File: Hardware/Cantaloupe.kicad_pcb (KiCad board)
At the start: 2 copper layers, 289.7 x 117 mm, 167 parts, among them J1 OLED, J2 Interconnect, J3 ICSP, J4 BAT_CON, J5 BAT_CON_R, J6 OLED, J7 Interconnect_R, J8 ICSP_R, J9 BAT_CON_TOG, SW1 MX, SW10 MX, SW11 MX, SW12 MX, SW13 MX, SW14 MX, SW15 MX, SW16 MX, SW17 MX, SW18 MX, SW19 MX, SW2 MX, SW20 MX, SW21 MX, SW22 MX, SW23 MX, SW24 MX, SW25 MX, SW26 MX, SW27 MX, SW28 MX, SW29 MX, SW3 MX, SW30 MX, SW31 MX, SW32 MX, SW33 Encoder, SW34 MX, SW35 Reset, SW36 BAT_TOG, SW37 MX, SW38 MX, SW39 MX, SW4 MX, SW40 MX, SW41 MX, SW42 MX, SW43 MX, SW44 MX, SW45 MX, SW46 MX, SW47 MX, SW48 MX, SW49 MX, SW5 MX, SW50 MX, SW51 MX, SW52 MX, SW53 MX, SW54 MX, SW55 MX, SW56 MX, SW57 MX, SW58 MX, SW59 MX, SW6 MX, SW60 MX, SW61 MX, SW62 MX, SW63 MX, SW64 MX, SW65 MX, SW66 MX, SW67 MX, SW68 MX, SW69 Encoder_R, SW7 MX, SW70 MX, SW71 Reset, SW72 BAT_TOG_R, SW8 MX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

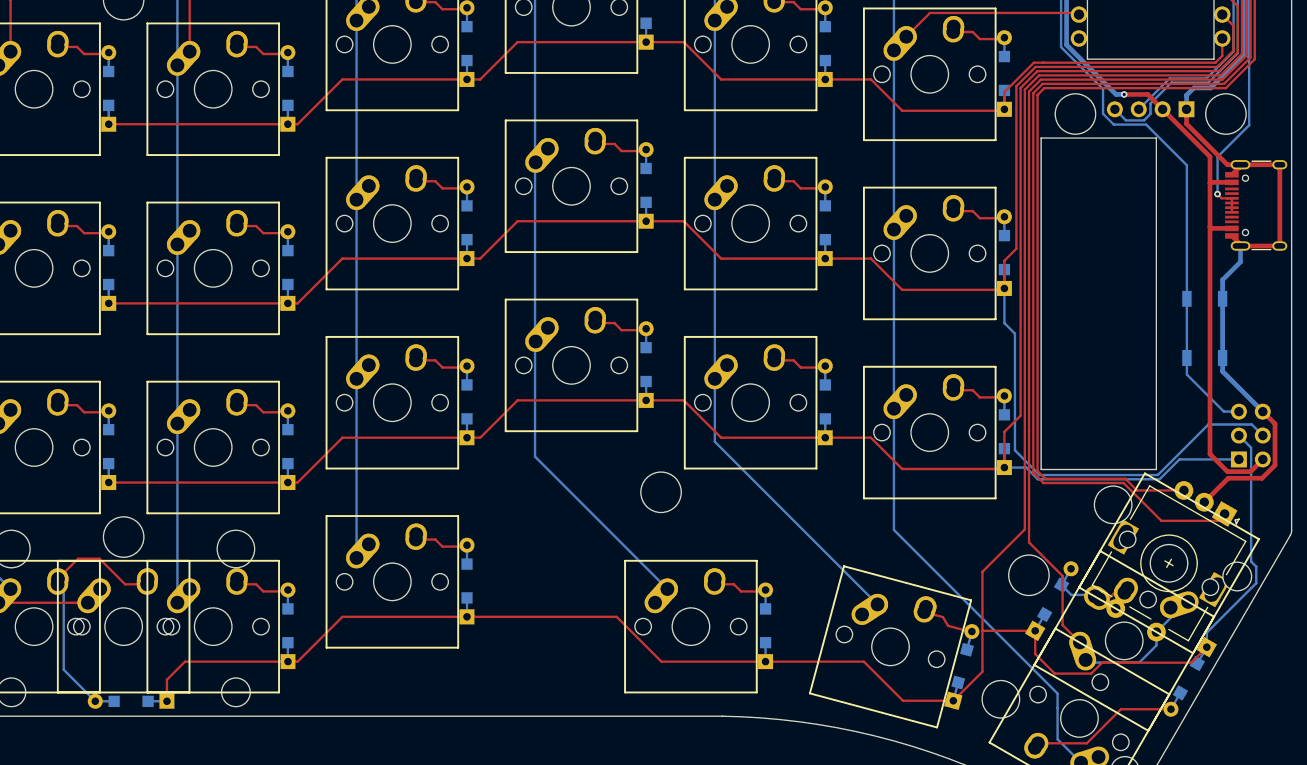
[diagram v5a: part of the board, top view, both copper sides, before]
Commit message: Updated position of diode
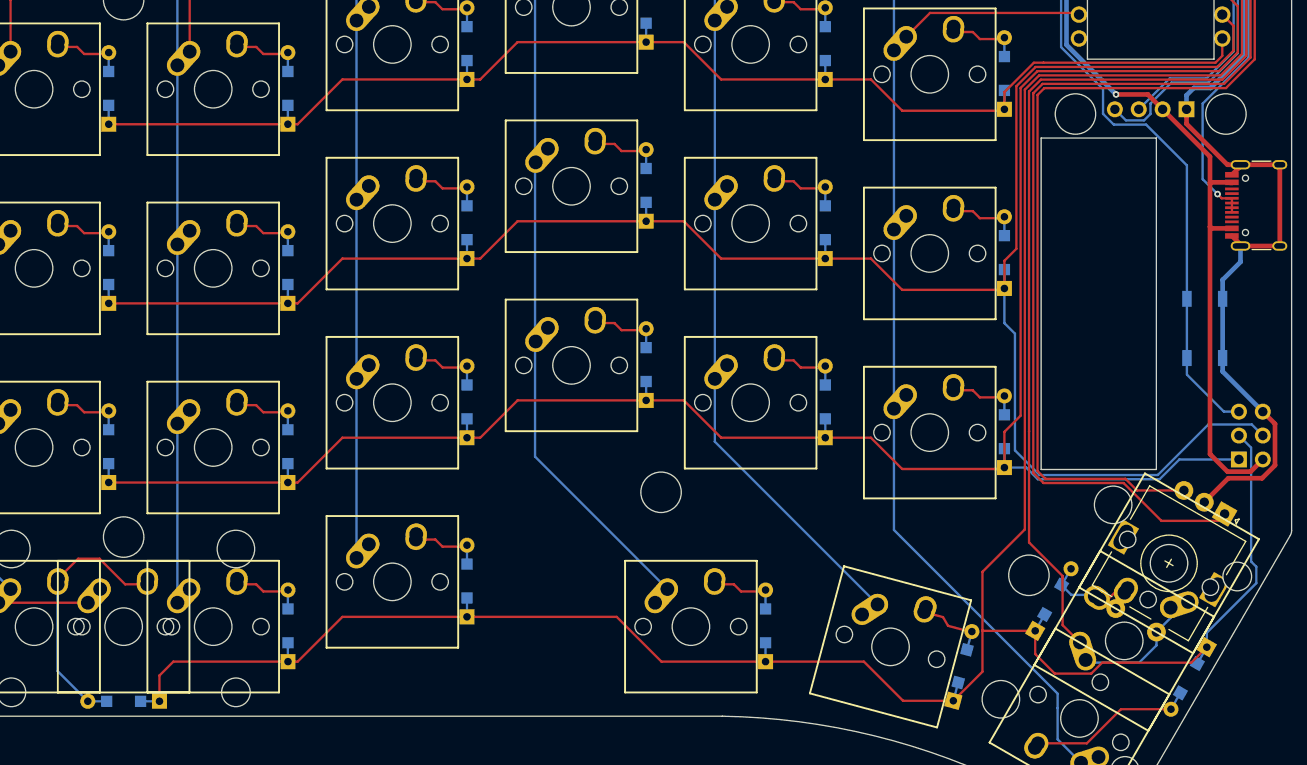
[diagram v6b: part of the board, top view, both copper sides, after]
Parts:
- moved D25 0.79 mm to (215.9, 134.9)
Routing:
- net DATA: track 47.7 -> 49.0 mm
- net ROW4: track 263.2 -> 264.3 mm

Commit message: Changed OLED support to 0.96" OLED
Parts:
- removed the REF** at (319.6, 92.7)
- removed the REF** at (333.1, 72.5)
- removed the REF** at (317.1, 72.5)
- removed the REF** at (70.9, 92.7)
- removed the REF** at (57.4, 72.5)
- removed the REF** at (73.4, 72.5)
- J1, J6: footprint Cantaloupe:PinHeader_1x04_P2.54mm_Vertical_No_Silk -> Cantaloupe:OLED_0.96_SSD1306_128x64
- SW35, SW71: moved to F.Cu
- moved J2 18.0 mm to (337.8, 100.2)
- moved J7 18.0 mm to (52.7, 100.2)
- moved SW35 7.07 mm to (325.9, 100.3)
- moved SW71 7.07 mm to (64.6, 100.3), turned to 270 degrees
- moved J8 6.98 mm to (57.8, 110.9), turned to 90 degrees
- moved J3 3.70 mm to (337.8, 110.9), turned to 90 degrees
- moved J6 3.56 mm to (64.2, 68.7), turned to 0 degrees
- moved J1 3.55 mm to (326.4, 68.7), turned to 0 degrees
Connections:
- U1 pad 4: GND1 -> Net-(U1-Pad4)
- U2 pad 4: GND2 -> Net-(U2-Pad4)
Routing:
- net GND1: track 101.8 -> 133.8 mm
- net GND2: track 140.7 -> 120.3 mm
- net ROW2: track 212.8 -> 196.5 mm
- net DATA: track 49.0 -> 64.8 mm
- net COL5_R: track 156.1 -> 142.1 mm
- net RESET: track 74.1 -> 86.5 mm, vias 0 -> 3
- net DATA_R: track 58.8 -> 70.9 mm
- net SDA: track 37.2 -> 25.6 mm
- net SDA_R: track 36.9 -> 27.4 mm
- net VDD: track 83.1 -> 74.0 mm, vias 0 -> 2
- net ROW4: track 264.3 -> 257.3 mm
- net COL4_R: track 172.0 -> 166.3 mm
- net RESET_R: track 82.0 -> 87.5 mm, vias 0 -> 4
- net SCL: track 29.7 -> 24.9 mm
- net VCC: track 85.3 -> 81.8 mm
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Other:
- board text removed: "OLED"

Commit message: Changed orientation of 1u switches in thumb cluster. Updated plate to add 2u support.
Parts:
- turned SW30 to 60 degrees
- turned SW34 to 60 degrees
- turned SW61 to 300 degrees
- turned SW70 to 300 degrees
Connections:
- SW34 pad 1: PERIPH -> Net-(D31-Pad2)
- SW34 pad 2: Net-(D31-Pad2) -> PERIPH
- SW70 pad 1: PERIPH_R -> Net-(D62-Pad2)
- SW70 pad 2: Net-(D62-Pad2) -> PERIPH_R
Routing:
- net PERIPH: track 109.9 -> 119.7 mm
- net Net-(D62-Pad2): track 22.7 -> 30.7 mm
- net COL5: track 122.5 -> 116.0 mm
- net Net-(D56-Pad2): track 14.9 -> 18.4 mm
- net ROW4: track 257.3 -> 259.9 mm
- net COL5_R: track 142.1 -> 139.7 mm
- net Net-(D30-Pad2): track 18.0 -> 15.8 mm
- net ROT_B_R: track 104.9 -> 106.9 mm
- net Net-(D31-Pad2): track 15.9 -> 14.4 mm
- net RESET_R: track 87.5 -> 86.3 mm, vias 4 -> 3
- net ROT_A: track 101.4 -> 102.5 mm
- net COL4_R: track 166.3 -> 166.9 mm
